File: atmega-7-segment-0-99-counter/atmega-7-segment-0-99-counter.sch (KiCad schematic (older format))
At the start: 52 parts, among them IC1 ATMEGA328P-P, P1 SPI, Q1 PN2222A, Q2 PN2222A, U1 74HC14, U2 LM7805CT, Y1 20MHz

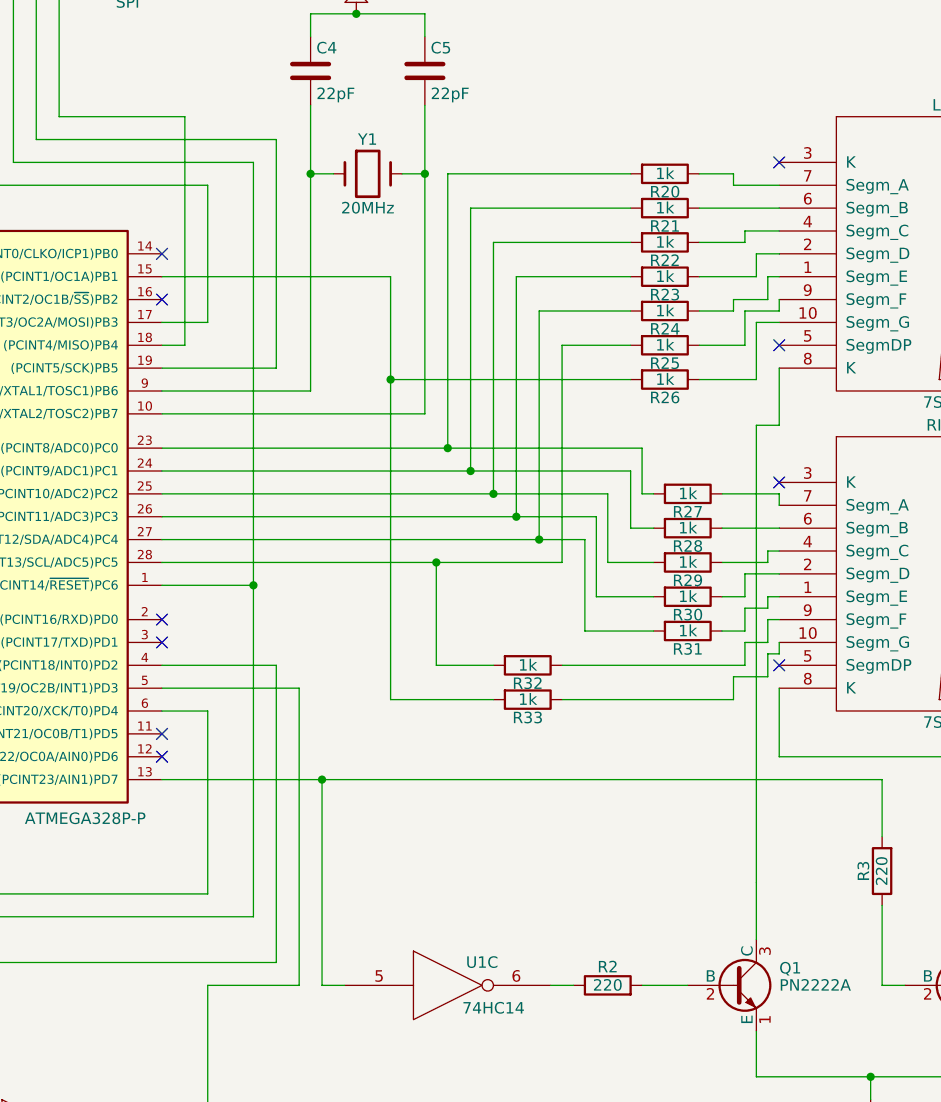
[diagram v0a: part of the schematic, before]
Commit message: Adjusted circuit to remove unnecessary Rs for 7-seg LED
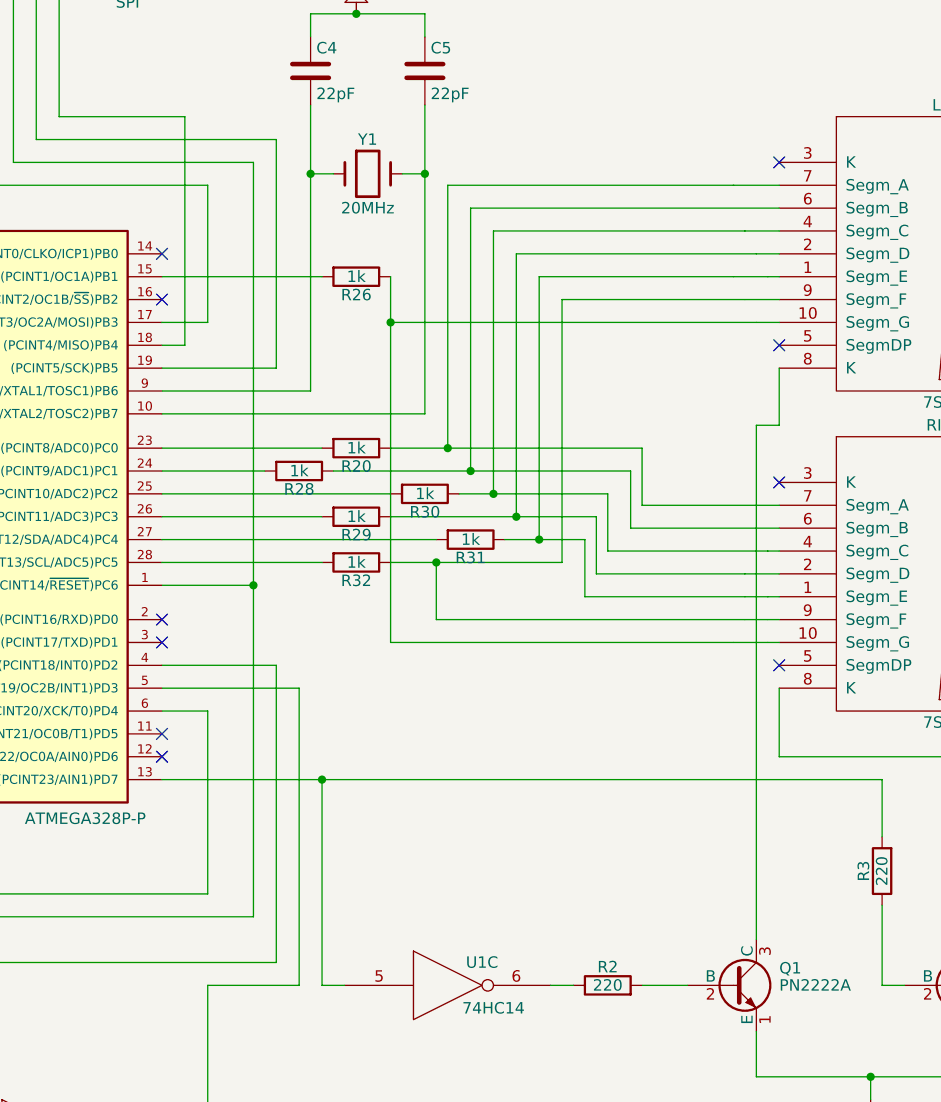
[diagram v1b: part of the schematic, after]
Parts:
- removed R21, R22, R23, R24, R25, R27, R33: 1k, symbol R
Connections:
- net at IC1.25 ((PCINT10/ADC2)PC2): now also R30.2; no longer R29.2
- net at IC1.26 ((PCINT11/ADC3)PC3): now also R29.2; no longer R30.2
- net at LEFT.1 (Segm_E): now also R31.1, RIGHT.1 (Segm_E)
- net at LEFT.10 (Segm_G), R26.1: now also RIGHT.10 (Segm_G)
- net at LEFT.2 (Segm_D): now also R29.1, RIGHT.2 (Segm_D)
- net at LEFT.4 (Segm_C): now also R30.1, RIGHT.4 (Segm_C)
- net at LEFT.6 (Segm_B): now also R28.1, RIGHT.6 (Segm_B)
- net at LEFT.7 (Segm_A), R20.1: now also RIGHT.7 (Segm_A)
- net at LEFT.9 (Segm_F): now also R32.1, RIGHT.9 (Segm_F)
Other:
- moved on the sheet: R20, R26, R28, R29, R30, R31, R32

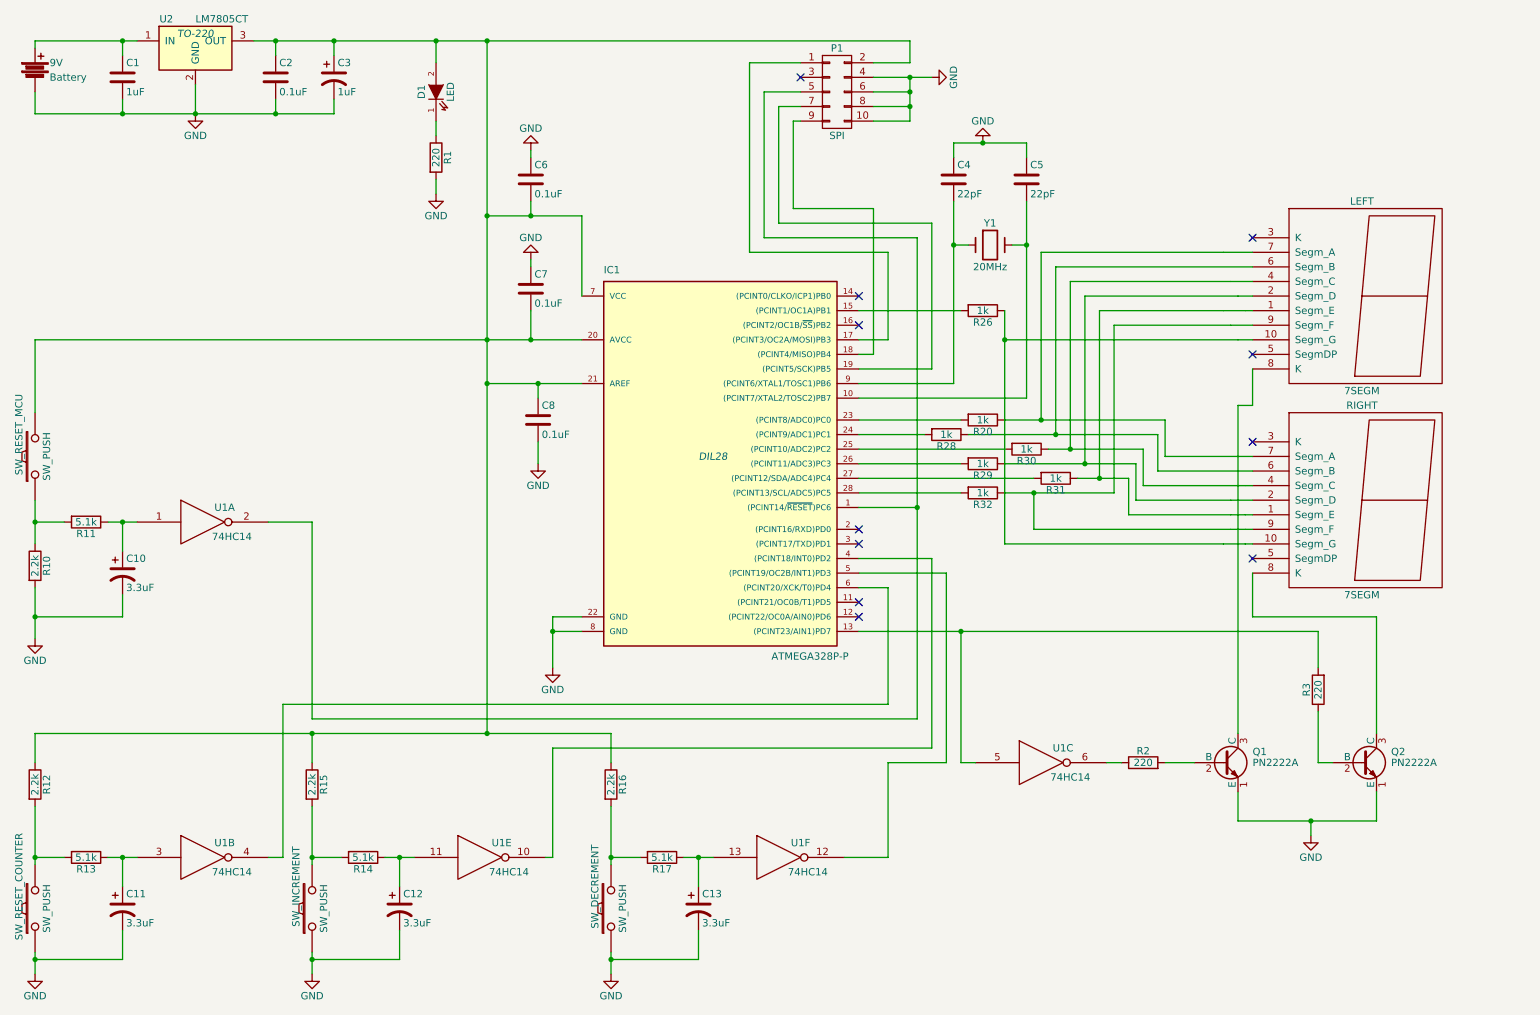
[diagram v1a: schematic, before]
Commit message: Added some footprints
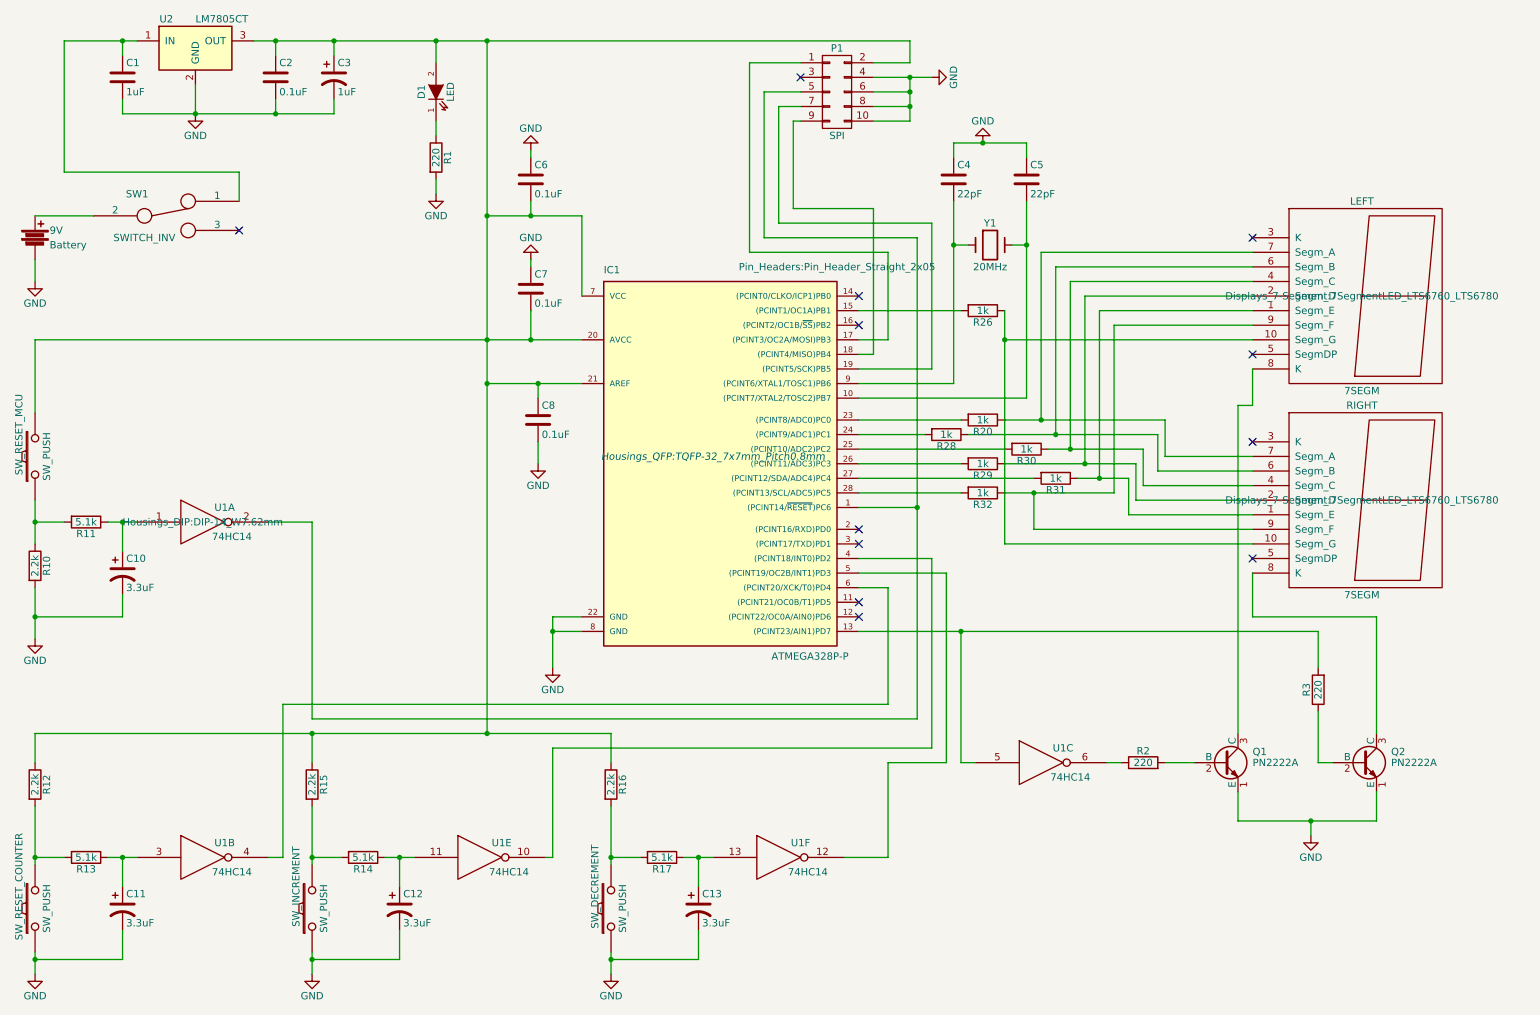
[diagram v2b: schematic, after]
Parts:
- added SW1: SWITCH_INV, symbol SWITCH_INV
- 9V: footprint (none) -> Terminal_Blocks:TerminalBlock_Pheonix_MKDS1.5-2pol
- IC1: footprint DIL28 -> Housings_QFP:TQFP-32_7x7mm_Pitch0.8mm
- LEFT, RIGHT: footprint (none) -> Displays_7-Segment:7SegmentLED_LTS6760_LTS6780
- P1: footprint (none) -> Pin_Headers:Pin_Header_Straight_2x05
- SW_DECREMENT, SW_INCREMENT, SW_RESET_COUNTER, SW_RESET_MCU: footprint (none) -> Buttons_Switches_ThroughHole:SW_PUSH_6mm
- U1: footprint (none) -> Housings_DIP:DIP-14_W7.62mm
- U2: footprint TO-220 -> TO_SOT_Packages_THT:TO-220_Neutral123_Vertical
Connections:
- net at C1.1, U2.1 (IN): now also SW1.1; no longer 9V.1
- new net: 9V.1, SW1.2
- no-connect marks 11 -> 12
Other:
- moved on the sheet: 9V
